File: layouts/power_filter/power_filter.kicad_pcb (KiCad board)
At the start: 2 copper layers, 10 parts

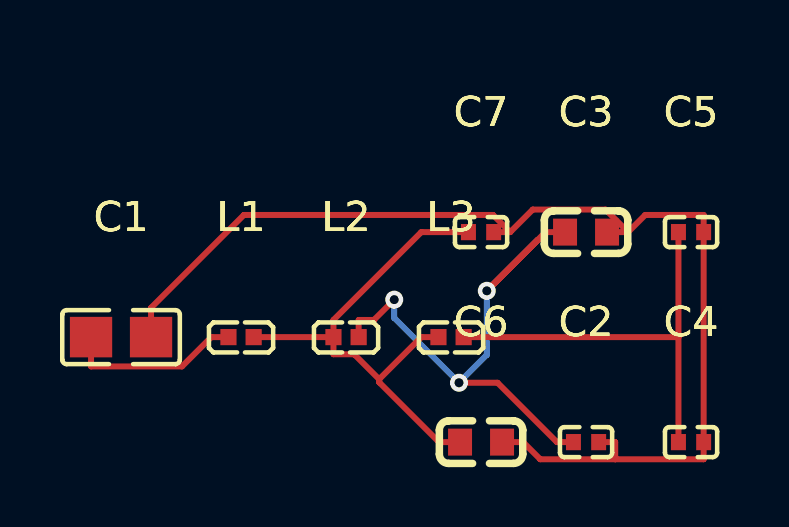
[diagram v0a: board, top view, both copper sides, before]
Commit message: Enhance smart placer with simulated annealing and pre-routing validation
Smart Placer improvements:
- Add simulated annealing refinement (now default) for better wire length optimization
- Add force-directed refinement with improvement safeguard
- Add silkscreen text repositioning to avoid component overlaps
- Significant wire length reductions (e.g., power_filter: 113mm -> 46mm)

Autorouter improvements:
- Add PreRoutingValidator class for pre-flight checks
- Validate unconnected pads, overlapping footprints, unplaced components
- Use pad-based bounds for accurate overlap detection
- Block routing on validation errors with actionable messages

Research:
- Add comprehensive autorouting/autoplacement findings document
- Cover Freerouting Python client, OrthoRoute, DeepPCB, KiCad 9 IPC API
- Document force-directed and simulated annealing algorithms

Cleanup:
- Update .gitignore for DSN/SES files, build artifacts, tools
- Remove stale timestamped build files
- Add parts footprints and symbols

All 10 modules placed and routed successfully.

Co-Authored-By: Claude Opus 4.5 <noreply@anthropic.com>
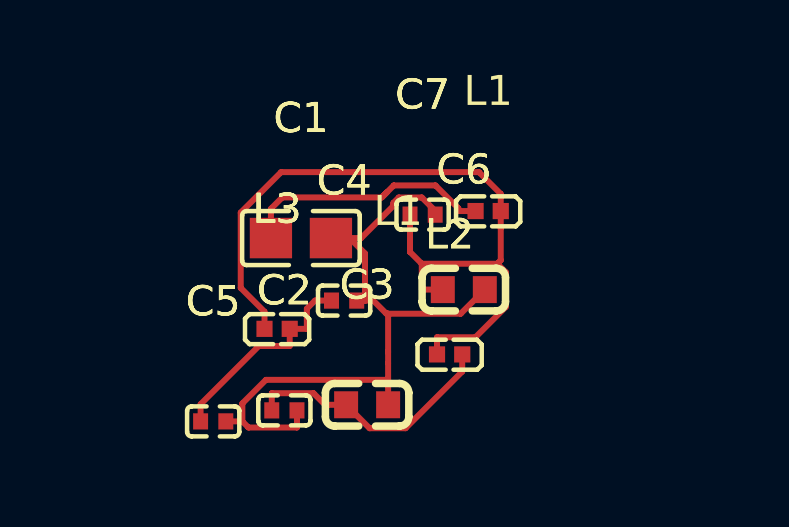
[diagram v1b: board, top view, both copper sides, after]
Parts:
- moved C5 17.1 mm to (91.1, 102.8)
- moved C4 12.5 mm to (95.4, 98.8)
- moved C2 10.1 mm to (93.4, 102.4)
- moved C3 9.29 mm to (96.2, 102.3)
- moved L1 9.25 mm to (100.2, 95.8)
- moved C1 6.85 mm to (94.0, 96.7)
- moved L3 5.80 mm to (93.2, 99.7)
- moved C6 5.12 mm to (99.4, 98.4)
- moved L2 3.50 mm to (99.0, 100.6)
- moved C7 2.03 mm to (98.1, 95.9)
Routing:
- net vcc_mcu: track 26.8 -> 8.76 mm, vias 3 -> 0
- net gnd: track 39.3 -> 23.3 mm
- net vcc: track 17.6 -> 26.8 mm
- net vcc_sensors: track 14.2 -> 7.10 mm
- net vbat: track 5.96 -> 8.76 mm
